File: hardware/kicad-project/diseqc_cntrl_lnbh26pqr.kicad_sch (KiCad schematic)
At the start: 18 parts, among them IC5 LNBH26PQR, J6 SMA_Sock, J7 SMA_Sock

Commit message: Corrective changes to power regulation: F1, PS1
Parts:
- C24, C26: footprint LIB_865080445010:CAPAE660X770N -> diseqc_cntrl:CAPAE660X770N
- C29: footprint GRM1885C2A221JA01D:CAPC1608X90N -> diseqc_cntrl:CAPC1608X90N
- D4: footprint STPS130A:STTH2R02AY -> diseqc_cntrl:STTH2R02AY
- D6: footprint LIB_BAT43XV2:SODFL1608X70N -> diseqc_cntrl:SODFL1608X70N
- D7: footprint RCLAMP0502BATCT:SOT50P160X90-3N -> diseqc_cntrl:SOT50P160X90-3N
- IC5: footprint LNBH26PQR:QFN50P400X400X100-25N-D -> diseqc_cntrl:QFN50P400X400X100-25N-D
- J6, J7: My Stock 0 -> (none)
- L5: footprint 0603DC-27NXJRW:0603DC27NXJRW -> diseqc_cntrl:0603DC27NXJRW
- NT2: My Stock 1000 -> (none)
- R16: My Stock 50 -> (none)
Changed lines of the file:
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@@
 			)
 		)
-		(property "Footprint" "0603DC-27NXJRW:0603DC27NXJRW"
+		(property "Footprint" "diseqc_cntrl:0603DC27NXJRW"
 			(at 191.77 163.5 0)
 			(effects
@@
 		)
 		(property "Mouser_Part_Number" ""
-			(at 175.26 67.31 0)
-			(effects
-				(font
-					(size 1.27 1.27)
-				)
-				(hide yes)
-			)
-		)
-		(property "My Stock" ""
 			(at 175.26 67.31 0)
 			(effects
@@
 		)
 		(property "Mouser Part Number" "791-0603B204K160CT"
-			(at 160.02 72.39 0)
-			(effects
-				(font
-					(size 1.27 1.27)
-				)
-				(hide yes)
-			)
-		)
-		(property "My Stock" ""
 			(at 160.02 72.39 0)
 			(effects
@@
 			)
 		)
-		(property "Footprint" "LNBH26PQR:QFN50P400X400X100-25N-D"
+		(property "Footprint" "diseqc_cntrl:QFN50P400X400X100-25N-D"
 			(at 157.48 172.39 0)
 			(effects
@@
 		)
 		(property "Mouser_Part_Number" ""
-			(at 120.65 90.17 0)
-			(effects
-				(font
-					(size 1.27 1.27)
-				)
-				(hide yes)
-			)
-		)
-		(property "My Stock" ""
 			(at 120.65 90.17 0)
 			(effects
@@
 			)
 		)
-		(property "My Stock" "0"
-			(at 215.9 55.88 0)
-			(effects
-				(font
-					(size 1.27 1.27)
-				)
-				(hide yes)
-			)
-		)
 		(property "Mouser Part Number" "538-73251-1153"
 			(at 215.9 55.88 0)
@@
 			)
 		)
-		(property "Footprint" "STPS130A:STTH2R02AY"
+		(property "Footprint" "diseqc_cntrl:STTH2R02AY"
 			(at 97.79 81.28 0)
 			(effects
@@
 		)
 		(property "Mouser Part Number" "511-STPS130A"
-			(at 97.79 81.28 90)
-			(effects
-				(font
-					(size 1.27 1.27)
-				)
-				(hide yes)
-			)
-		)
-		(property "My Stock" ""
 			(at 97.79 81.28 90)
 			(effects
@@
 			)
 		)
-		(property "My Stock" ""
-			(at 102.87 57.15 0)
-			(effects
-				(font
-					(size 1.27 1.27)
-				)
-				(hide yes)
-			)
-		)
 		(pin "2"
 		)
@@
 			)
 		)
-		(property "Footprint" "LIB_BAT43XV2:SODFL1608X70N"
+		(property "Footprint" "diseqc_cntrl:SODFL1608X70N"
 			(at 167.005 72.39 0)
 			(effects
@@
 		)
 		(property "Mouser Part Number" "512-BAT43XV2"
-			(at 171.45 72.39 90)
-			(effects
-				(font
-					(size 1.27 1.27)
-				)
-				(hide yes)
-			)
-		)
-		(property "My Stock" ""
 			(at 171.45 72.39 90)
 			(effects
@@
 			)
 		)
-		(property "My Stock" ""
-			(at 160.02 63.5 90)
-			(effects
-				(font
-					(size 1.27 1.27)
-				)
-				(hide yes)
-			)
-		)
 		(pin "1"
 		)
@@
 			)
 		)
-		(property "Footprint" "LIB_865080445010:CAPAE660X770N"
+		(property "Footprint" "diseqc_cntrl:CAPAE660X770N"
 			(at 26.3652 38.1 0)
 			(effects
@@
 		)
 		(property "Mouser Part Number" "710-865080445010"
-			(at 25.4 34.29 0)
-			(effects
-				(font
-					(size 1.27 1.27)
-				)
-				(hide yes)
-			)
-		)
-		(property "My Stock" ""
 			(at 25.4 34.29 0)
 			(effects
@@
 			)
 		)
-		(property "My Stock" "0"
-			(at 215.9 67.31 0)
-			(effects
-				(font
-					(size 1.27 1.27)
-				)
-				(hide yes)
-			)
-		)
 		(property "Mouser Part Number" "538-73251-1153"
 			(at 215.9 67.31 0)
@@
 			)
 		)
-		(property "Footprint" "RCLAMP0502BATCT:SOT50P160X90-3N"
+		(property "Footprint" "diseqc_cntrl:SOT50P160X90-3N"
 			(at 222.25 129.21 0)
 			(effects
@@
 		)
 		(property "Mouser_Part_Number" ""
-			(at 190.5 34.29 0)
-			(effects
-				(font
-					(size 1.27 1.27)
-				)
-				(hide yes)
-			)
-		)
-		(property "My Stock" ""
 			(at 190.5 34.29 0)
 			(effects
@@
 			)
 		)
-		(property "My Stock" ""
-			(at 187.96 100.33 0)
-			(effects
-				(font
-					(size 1.27 1.27)
-				)
-				(hide yes)
-			)
-		)
 		(pin "2"
 		)
@@
 		)
 		(property "Mouser_Part_Number" ""
-			(at 38.1 43.18 0)
-			(effects
-				(font
-					(size 1.27 1.27)
-				)
-				(hide yes)
-			)
-		)
-		(property "My Stock" "1000"
 			(at 38.1 43.18 0)
 			(effects
@@
 			)
 		)
-		(property "My Stock" "50"
-			(at 138.43 138.43 0)
-			(effects
-				(font
-					(size 1.27 1.27)
-				)
-				(hide yes)
-			)
-		)
 		(pin "1"
 		)
@@
 			)
 		)
-		(property "My Stock" ""
-			(at 175.26 100.33 0)
-			(effects
-				(font
-					(size 1.27 1.27)
-				)
-				(hide yes)
-			)
-		)
 		(pin "2"
 		)
@@
 			)
 		)
-		(property "Footprint" "GRM1885C2A221JA01D:CAPC1608X90N"
+		(property "Footprint" "diseqc_cntrl:CAPC1608X90N"
 			(at 189.23 152.07 0)
 			(effects
@@
 		)
 		(property "Mouser_Part_Number" ""
-			(at 180.34 55.88 0)
-			(effects
-				(font
-					(size 1.27 1.27)
-				)
-				(hide yes)
-			)
-		)
-		(property "My Stock" ""
 			(at 180.34 55.88 0)
 			(effects
@@
 			)
 		)
-		(property "Footprint" "LIB_865080445010:CAPAE660X770N"
+		(property "Footprint" "diseqc_cntrl:CAPAE660X770N"
 			(at 115.2652 60.96 0)
 			(effects
@@
 		)
 		(property "Mouser Part Number" "710-865080445010"
-			(at 114.3 57.15 0)
-			(effects
-				(font
-					(size 1.27 1.27)
-				)
-				(hide yes)
-			)
-		)
-		(property "My Stock" ""
 			(at 114.3 57.15 0)
 			(effects
@@
 			(at 102.87 95.25 90)
 			(effects
-				(font
-					(size 1.27 1.27)
-				)
-				(hide yes)
-			)
-		)
-		(property "My Stock" ""
-			(at 102.87 95.25 90)
-			(effects

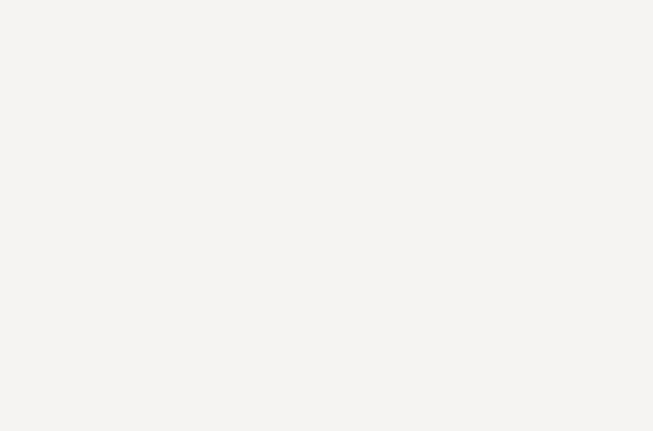
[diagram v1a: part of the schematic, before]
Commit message: Added more test points
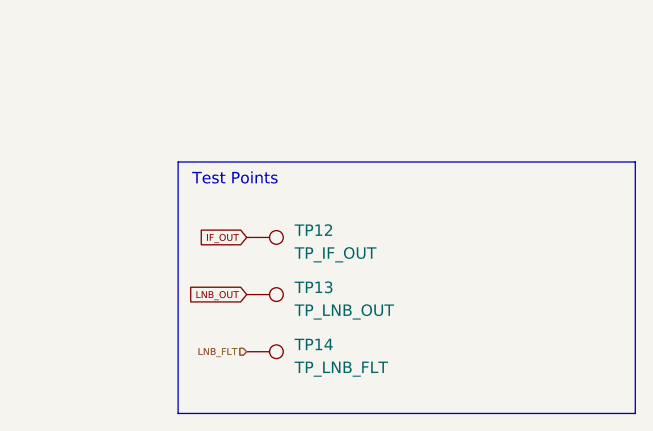
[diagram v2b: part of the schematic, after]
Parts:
- added TP12: TP_IF_OUT, TestPoint:TestPoint_THTPad_D1.0mm_Drill0.5mm, symbol Connector:TestPoint
- added TP13: TP_LNB_OUT, TestPoint:TestPoint_THTPad_D1.0mm_Drill0.5mm, symbol Connector:TestPoint
- added TP14: TP_LNB_FLT, TestPoint:TestPoint_THTPad_D1.0mm_Drill0.5mm, symbol Connector:TestPoint
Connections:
- net IF_OUT: now also TP12.1
- net LNB_FLT: now also TP14.1
- net LNB_OUT: now also TP13.1
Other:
- note added: "Test Points"

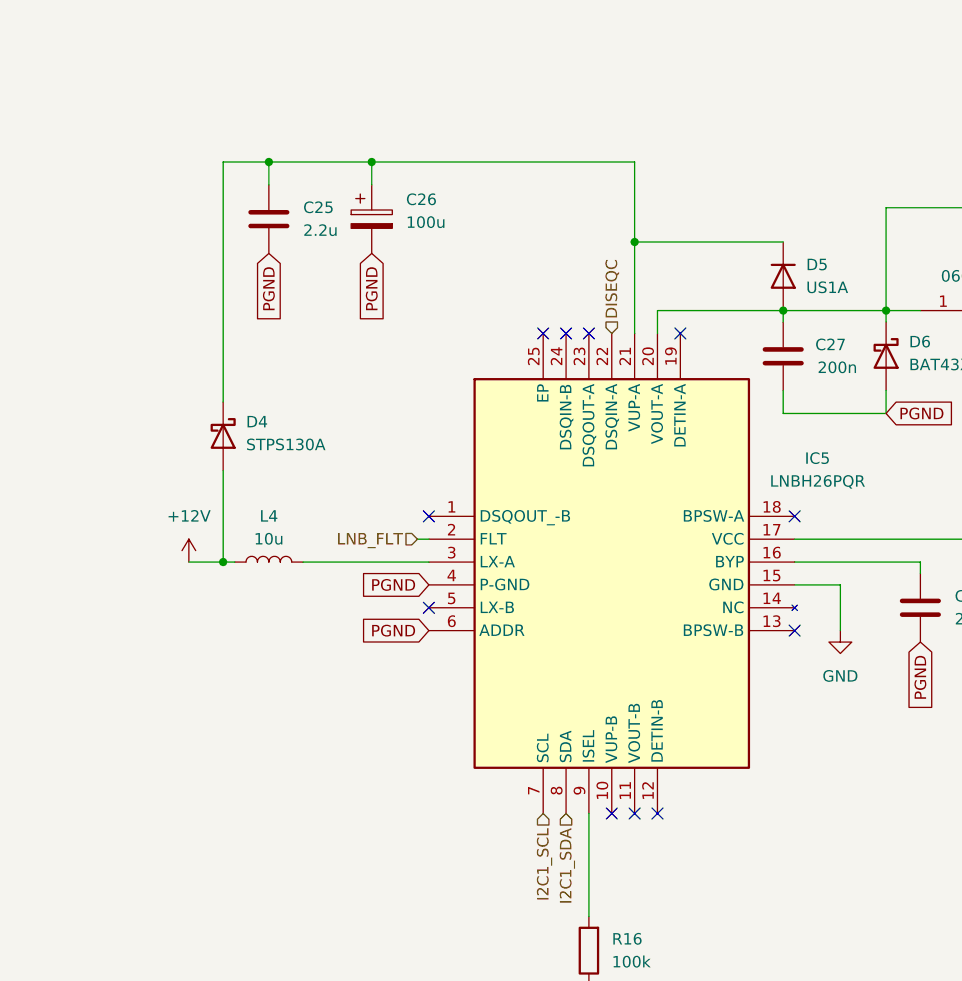
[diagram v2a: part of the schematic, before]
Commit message: Grounded additional pins on IC5 & cleaned up track routing
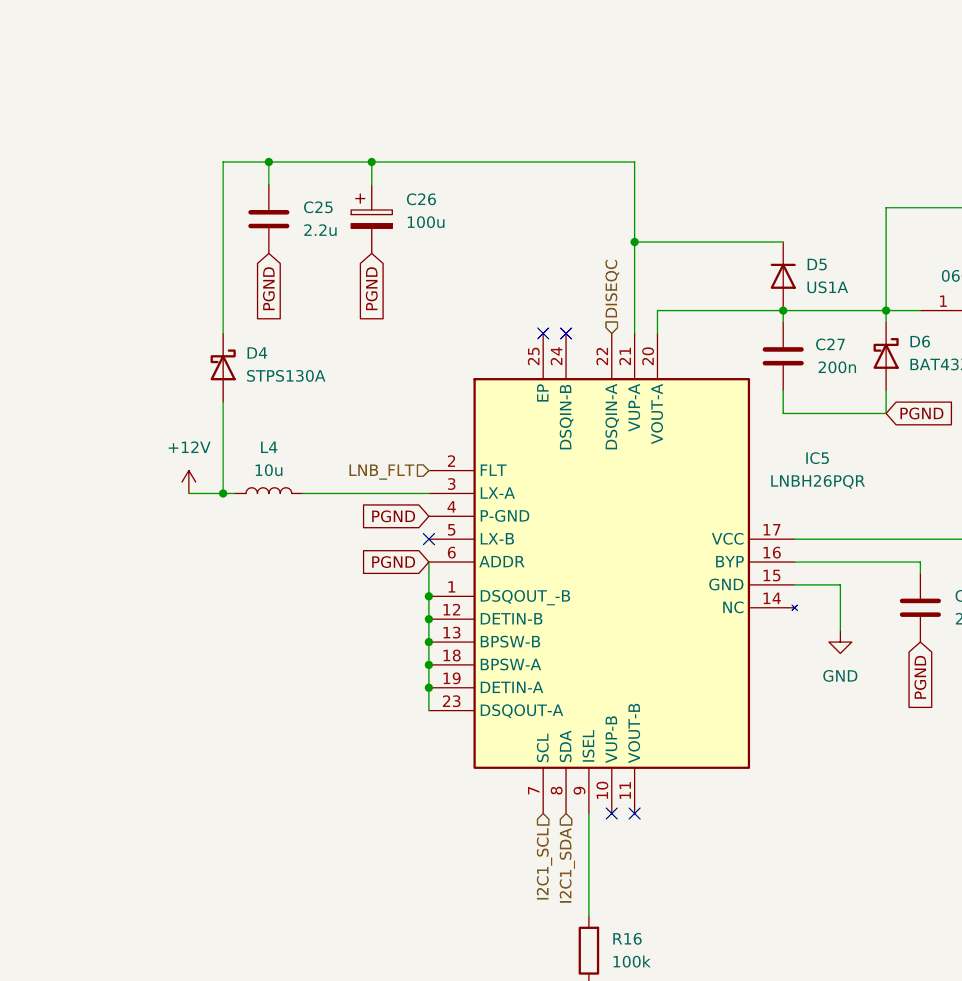
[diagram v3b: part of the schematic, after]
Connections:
- net PGND: now also IC5.1 (DSQOUT_-B), IC5.12 (DETIN-B), IC5.13 (BPSW-B), IC5.18 (BPSW-A), IC5.19 (DETIN-A), IC5.23 (DSQOUT-A)
- no-connect marks 12 -> 6
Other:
- moved on the sheet: D4, L4
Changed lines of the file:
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@@
 	)
 	(junction
+		(at 120.65 106.68)
+		(diameter 0)
+		(color 0 0 0 0)
+	)
+	(junction
+		(at 120.65 104.14)
+		(diameter 0)
+		(color 0 0 0 0)
+	)
+	(junction
 		(at 199.39 55.88)
 		(diameter 0)
@@
 	)
 	(junction
+		(at 120.65 99.06)
+		(diameter 0)
+		(color 0 0 0 0)
+	)
+	(junction
 		(at 220.98 55.88)
 		(diameter 0)
@@
 	)
 	(junction
+		(at 120.65 101.6)
+		(diameter 0)
+		(color 0 0 0 0)
+	)
+	(junction
 		(at 220.98 67.31)
 		(diameter 0)
@@
 	)
 	(junction
-		(at 97.79 95.25)
+		(at 97.79 87.63)
 		(diameter 0)
 		(color 0 0 0 0)
@@
 	)
 	(junction
+		(at 120.65 109.22)
+		(diameter 0)
+		(color 0 0 0 0)
+	)
+	(junction
 		(at 187.96 92.71)
 		(diameter 0)
@@
 	)
 	(no_connect
-		(at 161.29 102.87)
-	)
-	(no_connect
-		(at 120.65 90.17)
+		(at 120.65 92.71)
 	)
 	(no_connect
@@
 	)
 	(no_connect
-		(at 120.65 100.33)
-	)
-	(no_connect
 		(at 190.5 34.29)
 	)
 	(no_connect
-		(at 148.59 69.85)
-	)
-	(no_connect
 		(at 135.89 69.85)
 	)
 	(no_connect
-		(at 146.05 123.19)
-	)
-	(no_connect
-		(at 161.29 90.17)
-	)
-	(no_connect
-		(at 138.43 69.85)
-	)
-	(no_connect
 		(at 140.97 123.19)
 	)
@@
 	(wire
 		(pts
+			(xy 120.65 99.06) (xy 120.65 101.6)
+		)
+		(stroke
+			(width 0)
+			(type default)
+		)
+	)
+	(wire
+		(pts
 			(xy 160.02 67.31) (xy 171.45 67.31)
 		)
@@
 	(wire
 		(pts
-			(xy 97.79 50.8) (xy 102.87 50.8)
+			(xy 106.68 87.63) (xy 120.65 87.63)
 		)
 		(stroke
@@
 	(wire
 		(pts
-			(xy 160.02 67.31) (xy 160.02 68.58)
+			(xy 97.79 50.8) (xy 102.87 50.8)
 		)
 		(stroke
@@
 	(wire
 		(pts
-			(xy 106.68 95.25) (xy 120.65 95.25)
+			(xy 160.02 67.31) (xy 160.02 68.58)
 		)
 		(stroke
@@
 	(wire
 		(pts
+			(xy 120.65 109.22) (xy 120.65 111.76)
+		)
+		(stroke
+			(width 0)
+			(type default)
+		)
+	)
+	(wire
+		(pts
 			(xy 187.96 92.71) (xy 187.96 96.52)
 		)
@@
 	(wire
 		(pts
+			(xy 120.65 101.6) (xy 120.65 104.14)
+		)
+		(stroke
+			(width 0)
+			(type default)
+		)
+	)
+	(wire
+		(pts
 			(xy 161.29 95.25) (xy 175.26 95.25)
 		)
@@
 	(wire
 		(pts
-			(xy 93.98 95.25) (xy 97.79 95.25)
+			(xy 93.98 87.63) (xy 97.79 87.63)
 		)
 		(stroke
@@
 	(wire
 		(pts
+			(xy 120.65 106.68) (xy 120.65 109.22)
+		)
+		(stroke
+			(width 0)
+			(type default)
+		)
+	)
+	(wire
+		(pts
 			(xy 193.04 55.88) (xy 199.39 55.88)
 		)
@@
 	(wire
 		(pts
+			(xy 120.65 95.25) (xy 120.65 99.06)
+		)
+		(stroke
+			(width 0)
+			(type default)
+		)
+	)
+	(wire
+		(pts
 			(xy 175.26 95.25) (xy 175.26 96.52)
 		)
@@
 	(wire
 		(pts
-			(xy 97.79 77.47) (xy 97.79 50.8)
+			(xy 97.79 69.85) (xy 97.79 50.8)
 		)
 		(stroke
@@
 	(wire
 		(pts
-			(xy 119.38 92.71) (xy 120.65 92.71)
+			(xy 114.3 50.8) (xy 114.3 53.34)
 		)
 		(stroke
@@
 	(wire
 		(pts
-			(xy 114.3 50.8) (xy 114.3 53.34)
+			(xy 114.3 50.8) (xy 143.51 50.8)
 		)
 		(stroke
@@
 	(wire
 		(pts
-			(xy 114.3 50.8) (xy 143.51 50.8)
+			(xy 226.06 34.29) (xy 226.06 55.88)
 		)
 		(stroke
@@
 	(wire
 		(pts
-			(xy 226.06 34.29) (xy 226.06 55.88)
+			(xy 171.45 76.2) (xy 171.45 78.74)
 		)
 		(stroke
@@
 	(wire
 		(pts
-			(xy 171.45 76.2) (xy 171.45 78.74)
+			(xy 138.43 123.19) (xy 138.43 134.62)
 		)
 		(stroke
@@
 	(wire
 		(pts
-			(xy 138.43 123.19) (xy 138.43 134.62)
+			(xy 97.79 77.47) (xy 97.79 87.63)
 		)
 		(stroke
@@
 	(wire
 		(pts
-			(xy 97.79 85.09) (xy 97.79 95.25)
+			(xy 120.65 104.14) (xy 120.65 106.68)
 		)
 		(stroke
@@
 	(wire
 		(pts
-			(xy 97.79 95.25) (xy 99.06 95.25)
+			(xy 97.79 87.63) (xy 99.06 87.63)
 		)
 		(stroke
@@
 	(global_label "PGND"
 		(shape input)
-		(at 120.65 97.79 180)
+		(at 120.65 90.17 180)
 		(fields_autoplaced yes)
 		(effects
@@
 		)
 		(property "Intersheetrefs" "${INTERSHEET_REFS}"
-			(at 113.1785 97.79 0)
+			(at 113.1785 90.17 0)
 			(effects
 				(font
@@
 	(global_label "PGND"
 		(shape input)
-		(at 120.65 102.87 180)
+		(at 120.65 95.25 180)
 		(fields_autoplaced yes)
 		(effects
@@
 		)
 		(property "Intersheetrefs" "${INTERSHEET_REFS}"
-			(at 113.1785 102.87 0)
+			(at 113.1785 95.25 0)
 			(effects
 				(font
@@
 	(hierarchical_label "LNB_FLT"
 		(shape input)
-		(at 119.38 92.71 180)
+		(at 120.65 85.09 180)
 		(effects
 			(font
@@
 	(symbol
 		(lib_id "diseqc_cntrl:D_Schottky")
-		(at 97.79 81.28 270)
+		(at 97.79 73.66 270)
 		(unit 1)
 		(exclude_from_sim no)
@@
 		(fields_autoplaced yes)
 		(property "Reference" "D4"
-			(at 100.33 79.6924 90)
+			(at 100.33 72.0724 90)
 			(effects
 				(font
@@
 		)
 		(property "Value" "STPS130A"
-			(at 100.33 82.2324 90)
+			(at 100.33 74.6124 90)
 			(effects
 				(font
@@
 		)
 		(property "Footprint" "diseqc_cntrl:STTH2R02AY"
-			(at 97.79 81.28 0)
+			(at 97.79 73.66 0)
 			(effects
 				(font
@@
 		)
 		(property "Datasheet" "https://www.st.com/resource/en/datasheet/stps130.pdf"
-			(at 97.79 81.28 0)
+			(at 97.79 73.66 0)
 			(effects
 				(font
@@
 		)
 		(property "Description" "Schottky diode"
-			(at 97.79 81.28 0)
+			(at 97.79 73.66 0)
 			(effects
 				(font
@@
 		)
 		(property "Maufacturer_Part_Number" ""
-			(at 97.79 81.28 90)
+			(at 97.79 73.66 90)
 			(effects
 				(font
@@
 		)
 		(property "Manufacturer_Part_Code" ""
-			(at 97.79 81.28 90)
+			(at 97.79 73.66 90)
 			(effects
 				(font
@@
 		)
 		(property "Mouser_Part_Number" ""
-			(at 97.79 81.28 90)
+			(at 97.79 73.66 90)
 			(effects
 				(font
@@
 		)
 		(property "Mouser Part Number" "511-STPS130A"
-			(at 97.79 81.28 90)
+			(at 97.79 73.66 90)
 			(effects
 				(font
@@
 	(symbol
 		(lib_id "diseqc_cntrl:+12V")
-		(at 93.98 95.25 0)
+		(at 93.98 87.63 0)
 		(unit 1)
 		(exclude_from_sim no)
@@
 		(fields_autoplaced yes)
 		(property "Reference" "#PWR044"
-			(at 93.98 99.06 0)
+			(at 93.98 91.44 0)
 			(effects
 				(font
@@
 		)
 		(property "Value" "+12V"
-			(at 93.98 90.17 0)
+			(at 93.98 82.55 0)
 			(effects
 				(font
@@
 		)
 		(property "Footprint" ""
-			(at 93.98 95.25 0)
+			(at 93.98 87.63 0)
 			(effects
 				(font
@@
 		)
 		(property "Datasheet" ""
-			(at 93.98 95.25 0)
+			(at 93.98 87.63 0)
 			(effects
 				(font
@@
 		)
 		(property "Description" "Power symbol creates a global label with name \"+12V\""
-			(at 93.98 95.25 0)
+			(at 93.98 87.63 0)
 			(effects
 				(font
@@
 	(symbol
 		(lib_id "diseqc_cntrl:L")
-		(at 102.87 95.25 90)
+		(at 102.87 87.63 90)
 		(unit 1)
 		(exclude_from_sim no)
@@
 		(fields_autoplaced yes)
 		(property "Reference" "L4"
-			(at 102.87 90.17 90)
+			(at 102.87 82.55 90)
 			(effects
 				(font
@@
 		)
 		(property "Value" "10u"
-			(at 102.87 92.71 90)
+			(at 102.87 85.09 90)
 			(effects
 				(font
@@
 		)
 		(property "Footprint" "Inductor_SMD:L_0603_1608Metric_Pad1.05x0.95mm_HandSolder"
-			(at 102.87 95.25 0)
+			(at 102.87 87.63 0)
 			(effects
 				(font
@@
 		)
 		(property "Datasheet" "~"
-			(at 102.87 95.25 0)
+			(at 102.87 87.63 0)
 			(effects
 				(font
@@
 		)
 		(property "Description" "Inductor"
-			(at 102.87 95.25 0)
+			(at 102.87 87.63 0)
 			(effects
 				(font
@@
 		)
 		(property "Maufacturer_Part_Number" ""
-			(at 102.87 95.25 90)
+			(at 102.87 87.63 90)
 			(effects
 				(font
@@
 		)
 		(property "Manufacturer_Part_Code" ""
-			(at 102.87 95.25 90)
+			(at 102.87 87.63 90)
 			(effects
 				(font
@@
 		)
 		(property "Mouser_Part_Number" ""
-			(at 102.87 95.25 90)
+			(at 102.87 87.63 90)
 			(effects
 				(font
@@
 		)
 		(property "Mouser Part Number" "963-CBMF1608T100K"
-			(at 102.87 95.25 90)
+			(at 102.87 87.63 90)
 			(effects
 				(font

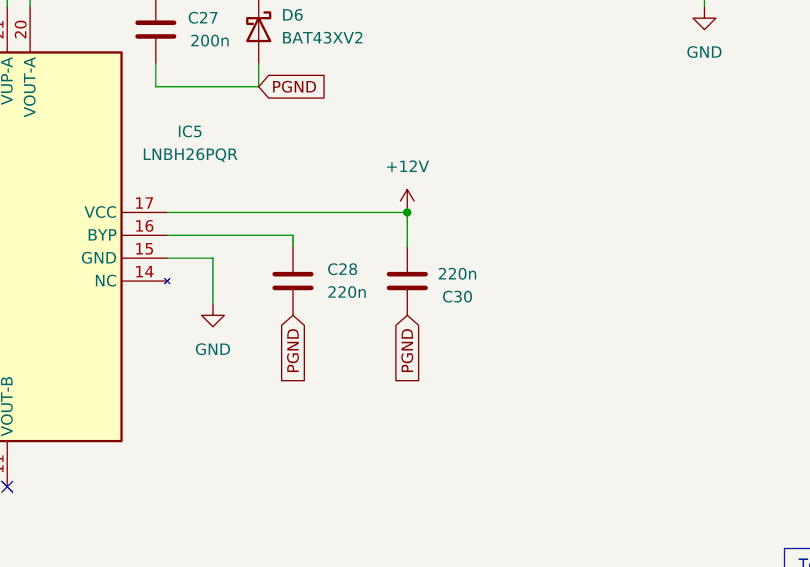
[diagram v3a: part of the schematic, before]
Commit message: Starting v0.4 with FT230 fixes; extra TPs
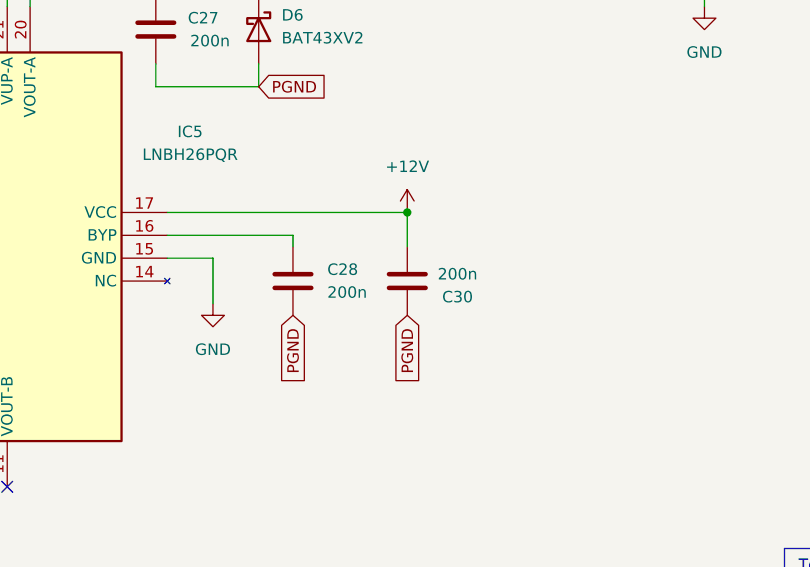
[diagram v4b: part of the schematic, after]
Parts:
- C24, C26: InvenTree Part (none) -> C_100u_Electrolytic
- C25: InvenTree Part (none) -> C_2u2_0603
- C27: InvenTree Part (none) -> C_200n_0603
- C28, C30: value 220n -> 200n; InvenTree Part (none) -> C_200n_0603
- C29: InvenTree Part (none) -> C_220p_0603
- D4: InvenTree Part (none) -> D_Schottky_1A_30V_SMA
- D5: InvenTree Part (none) -> D_FastRect_1A_50V_SMA
- D6: InvenTree Part (none) -> D_Schottky_BAT43
- D7: InvenTree Part (none) -> D_ESD_5V_SOT_523_3
- IC5: InvenTree Part (none) -> IC_LNB_CONTROL_13-18V_22kHz_QFN
- J6, J7: InvenTree Part (none) -> J_RF_SMA_SKT
- L4: InvenTree Part (none) -> L_10u_0603
- L5: InvenTree Part (none) -> L_27n_0603
- R16: InvenTree Part (none) -> R_100k_0603
- TP12, TP13, TP14: now left out of the parts list
